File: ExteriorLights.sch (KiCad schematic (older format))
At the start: 28 parts, among them J1 Left_Signal, J2 Right_Signal, J3 Brake Light, J4 Headlight, U1 EL3H7, U2 EL3H7, U3 EL3H7, U4 EL3H7

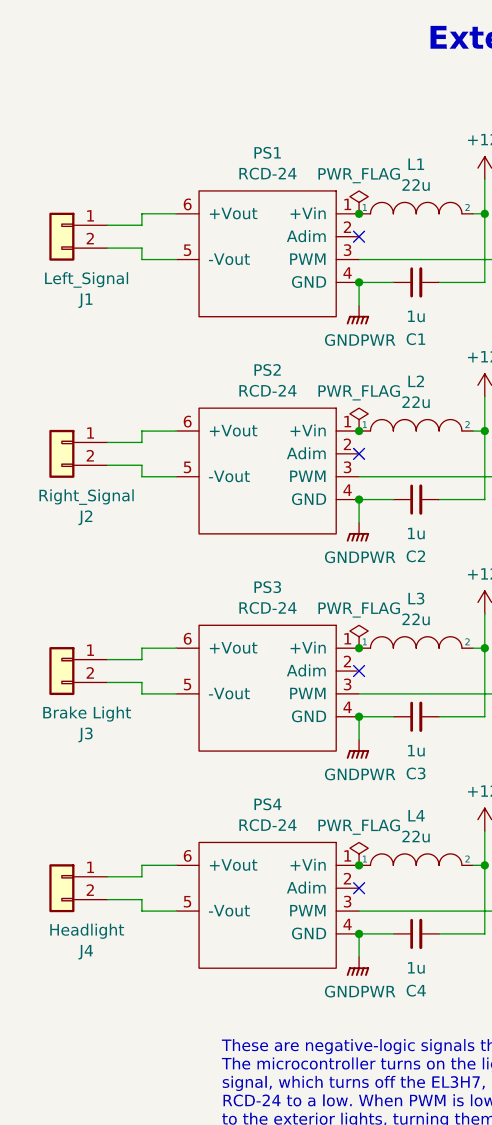
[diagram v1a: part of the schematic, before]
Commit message: Flips exterior lights polarity on the connectors
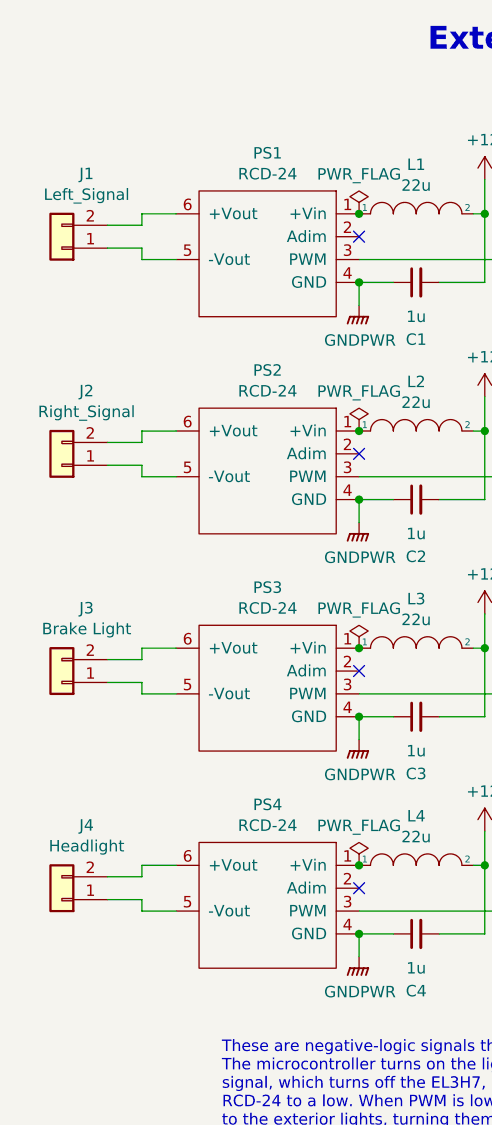
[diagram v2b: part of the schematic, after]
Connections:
- net at J1.1 (Pin_1): now also PS1.5 (-Vout); no longer PS1.6 (+Vout)
- net at J1.2 (Pin_2): now also PS1.6 (+Vout); no longer PS1.5 (-Vout)
- net at J2.1 (Pin_1): now also PS2.5 (-Vout); no longer PS2.6 (+Vout)
- net at J2.2 (Pin_2): now also PS2.6 (+Vout); no longer PS2.5 (-Vout)
- net at J3.1 (Pin_1): now also PS3.5 (-Vout); no longer PS3.6 (+Vout)
- net at J3.2 (Pin_2): now also PS3.6 (+Vout); no longer PS3.5 (-Vout)
- net at J4.1 (Pin_1): now also PS4.5 (-Vout); no longer PS4.6 (+Vout)
- net at J4.2 (Pin_2): now also PS4.6 (+Vout); no longer PS4.5 (-Vout)
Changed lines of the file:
@@
 L Connector_Generic:Conn_01x02 J1
 U 1 1 5F8A4005
-P 3550 2300
-F 0 "J1" H 3442 1975 50  0000 C CNN
-F 1 "Left_Signal" H 3442 2066 50  0000 C CNN
-F 2 "UTSVT_Connectors:Molex_MicroFit3.0_1x2xP3.00mm_PolarizingPeg_Vertical" H 3550 2300 50  0001 C CNN
-F 3 "~" H 3550 2300 50  0001 C CNN
-	1    3550 2300
-	-1   0    0    -1
+P 3550 2400
+F 0 "J1" H 3442 2075 50  0000 C CNN
+F 1 "Left_Signal" H 3442 2166 50  0000 C CNN
+F 2 "UTSVT_Connectors:Molex_MicroFit3.0_1x2xP3.00mm_PolarizingPeg_Vertical" H 3550 2400 50  0001 C CNN
+F 3 "~" H 3550 2400 50  0001 C CNN
+	1    3550 2400
+	-1   0    0    1
 $EndComp
 Wire Wire Line
@@
 L Connector_Generic:Conn_01x02 J2
 U 1 1 5F8A404F
-P 3550 3250
-F 0 "J2" H 3442 2925 50  0000 C CNN
-F 1 "Right_Signal" H 3442 3016 50  0000 C CNN
-F 2 "UTSVT_Connectors:Molex_MicroFit3.0_1x2xP3.00mm_PolarizingPeg_Vertical" H 3550 3250 50  0001 C CNN
-F 3 "~" H 3550 3250 50  0001 C CNN
-	1    3550 3250
-	-1   0    0    -1
+P 3550 3350
+F 0 "J2" H 3442 3025 50  0000 C CNN
+F 1 "Right_Signal" H 3442 3116 50  0000 C CNN
+F 2 "UTSVT_Connectors:Molex_MicroFit3.0_1x2xP3.00mm_PolarizingPeg_Vertical" H 3550 3350 50  0001 C CNN
+F 3 "~" H 3550 3350 50  0001 C CNN
+	1    3550 3350
+	-1   0    0    1
 $EndComp
 Wire Wire Line
@@
 L Connector_Generic:Conn_01x02 J3
 U 1 1 5F8A4098
-P 3550 4200
-F 0 "J3" H 3442 3875 50  0000 C CNN
-F 1 "Brake Light" H 3442 3966 50  0000 C CNN
-F 2 "UTSVT_Connectors:Molex_MicroFit3.0_1x2xP3.00mm_PolarizingPeg_Vertical" H 3550 4200 50  0001 C CNN
-F 3 "~" H 3550 4200 50  0001 C CNN
-	1    3550 4200
-	-1   0    0    -1
+P 3550 4300
+F 0 "J3" H 3442 3975 50  0000 C CNN
+F 1 "Brake Light" H 3442 4066 50  0000 C CNN
+F 2 "UTSVT_Connectors:Molex_MicroFit3.0_1x2xP3.00mm_PolarizingPeg_Vertical" H 3550 4300 50  0001 C CNN
+F 3 "~" H 3550 4300 50  0001 C CNN
+	1    3550 4300
+	-1   0    0    1
 $EndComp
 Wire Wire Line
@@
 L Connector_Generic:Conn_01x02 J4
 U 1 1 5F8A40E1
-P 3550 5150
-F 0 "J4" H 3442 4825 50  0000 C CNN
-F 1 "Headlight" H 3442 4916 50  0000 C CNN
-F 2 "UTSVT_Connectors:Molex_MicroFit3.0_1x2xP3.00mm_PolarizingPeg_Vertical" H 3550 5150 50  0001 C CNN
-F 3 "~" H 3550 5150 50  0001 C CNN
-	1    3550 5150
-	-1   0    0    -1
-$EndComp
-Wire Wire Line
+P 3550 5250
+F 0 "J4" H 3442 4925 50  0000 C CNN
+F 1 "Headlight" H 3442 5016 50  0000 C CNN
+F 2 "UTSVT_Connectors:Molex_MicroFit3.0_1x2xP3.00mm_PolarizingPeg_Vertical" H 3550 5250 50  0001 C CNN
+F 3 "~" H 3550 5250 50  0001 C CNN
+	1    3550 5250
+	-1   0    0    1
+$EndComp
+Wire Wire Line
